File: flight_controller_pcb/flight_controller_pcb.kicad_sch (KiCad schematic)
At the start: 53 parts, among them J1 Conn_01x08, J2 Conn_01x05, J3 Conn_01x02, U1 NRF24L01P-R7, U2 a, U3 STM32F411CEUx, U4 RFX2401C, U5 BMP390, U6 MPU-6500, U7 2450LP14A0100001T, U8 ICM-20948, Y1 Crystal_GND24

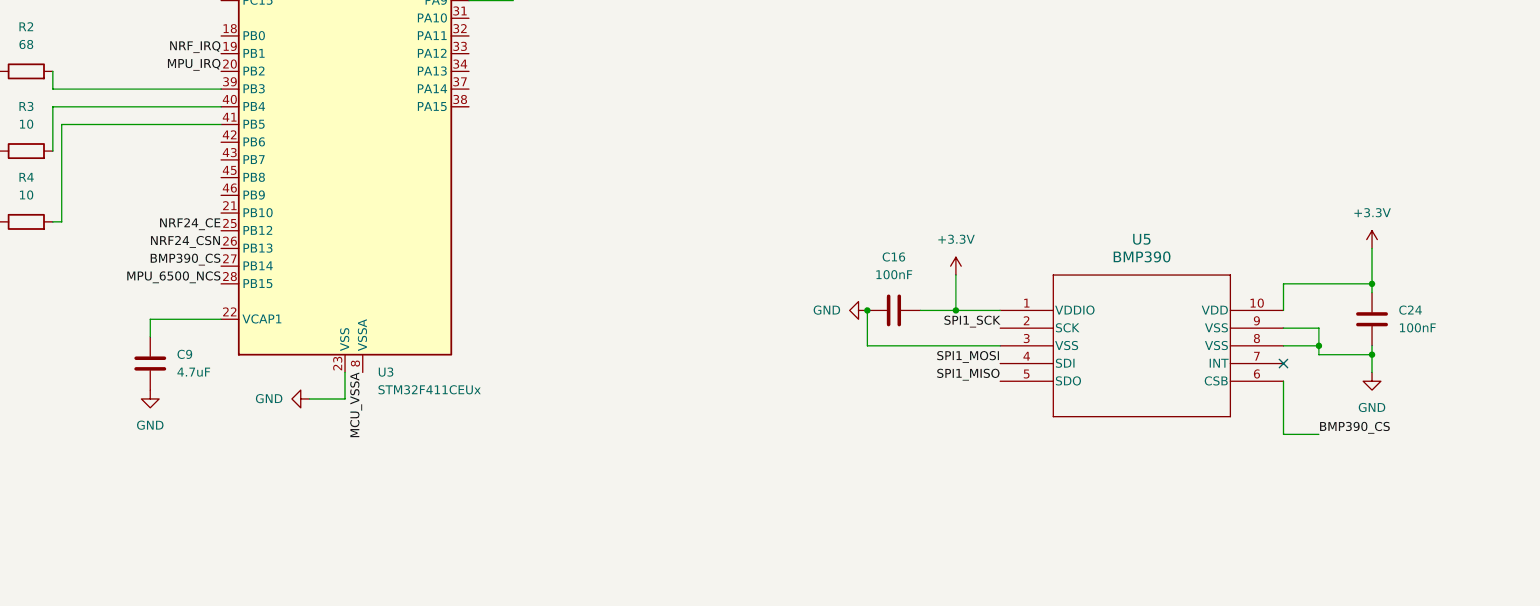
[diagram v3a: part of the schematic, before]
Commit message: Adde interrupt line for bmp390
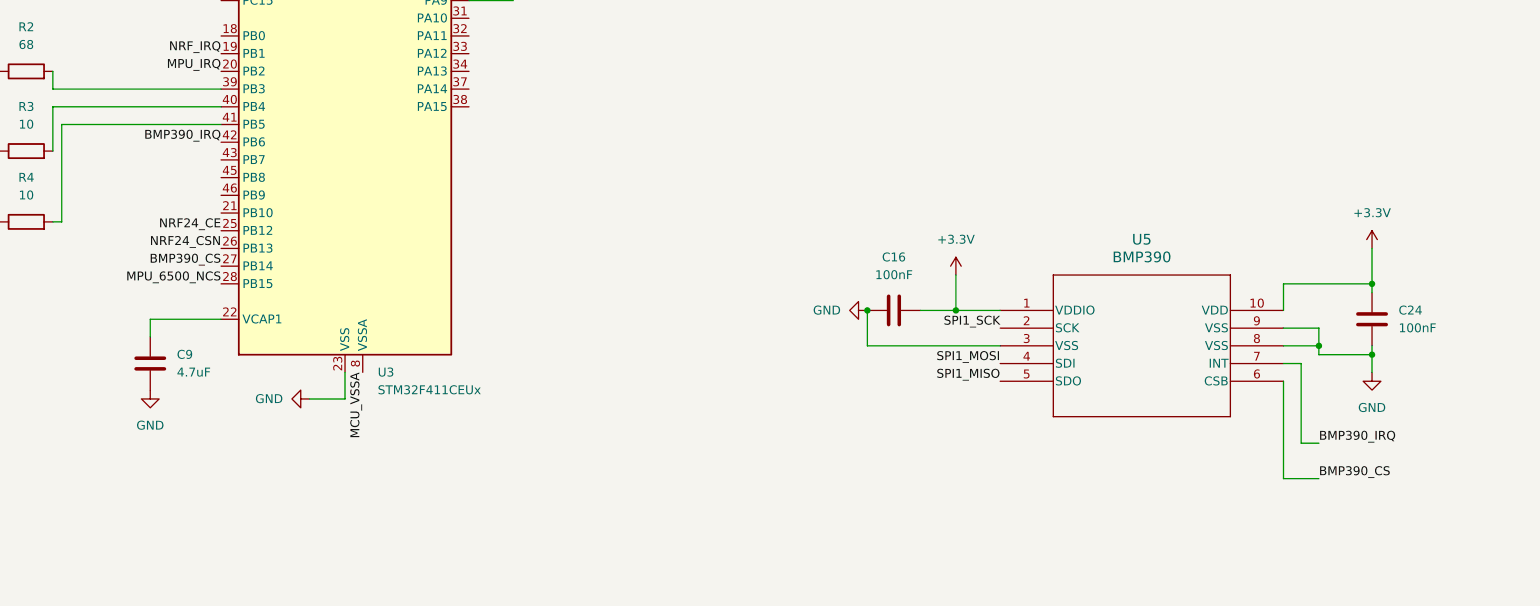
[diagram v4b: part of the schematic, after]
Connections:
- net BMP390_IRQ: now reaches U3.42 (PB6)
- net BMP390_IRQ: now also U5.7 (INT)
- no-connect marks 8 -> 7
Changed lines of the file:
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@@
-	)
-	(no_connect
-		(at 275.59 139.7)
 	)
 	(no_connect
@@
 	(wire
 		(pts
+			(xy 280.67 151.13) (xy 278.13 151.13)
+		)
+		(stroke
+			(width 0)
+			(type default)
+		)
+	)
+	(wire
+		(pts
 			(xy 99.06 109.22) (xy 99.06 102.87)
 		)
@@
 	(wire
 		(pts
-			(xy 275.59 149.86) (xy 280.67 149.86)
+			(xy 275.59 156.21) (xy 280.67 156.21)
 		)
 		(stroke
@@
 	(wire
 		(pts
+			(xy 278.13 139.7) (xy 275.59 139.7)
+		)
+		(stroke
+			(width 0)
+			(type default)
+		)
+	)
+	(wire
+		(pts
 			(xy 82.55 50.8) (xy 87.63 50.8)
 		)
@@
 	(wire
 		(pts
+			(xy 278.13 151.13) (xy 278.13 139.7)
+		)
+		(stroke
+			(width 0)
+			(type default)
+		)
+	)
+	(wire
+		(pts
 			(xy 275.59 53.34) (xy 274.32 53.34)
 		)
@@
 	(wire
 		(pts
-			(xy 275.59 142.24) (xy 275.59 149.86)
+			(xy 275.59 142.24) (xy 275.59 156.21)
 		)
 		(stroke
@@
 		)
 	)
+	(label "BMP390_IRQ"
+		(at 123.19 107.95 180)
+		(effects
+			(font
+				(size 1.27 1.27)
+			)
+			(justify right bottom)
+		)
+	)
 	(label "SPI1_SCK"
 		(at 165.1 77.47 0)
@@
 	)
 	(label "BMP390_CS"
-		(at 280.67 149.86 0)
+		(at 280.67 156.21 0)
 		(effects
 			(font
@@
 		(effects
 			(font
+				(size 1.27 1.27)
+			)
+			(justify left bottom)
+		)
+	)
+	(label "BMP390_IRQ"
+		(at 280.67 151.13 0)
+		(effects
+			(font

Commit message: ALOT of work on the PCB
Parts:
- removed D2: LED_KGBR, symbol Device:LED_KGBR
- removed R4: 10, Resistor_SMD:R_0402_1005Metric, symbol Device:R
- removed U6: MPU-6500, MPU-6500:QFN40P300X300X95-25N, symbol MPU-6500:MPU-6500
- added C25, C26, C27, C28, C29, C30, C31: 0.1uF, Capacitor_SMD:C_0402_1005Metric, symbol Device:C
- added D2, D4: LED, LED_SMD:LED_0402_1005Metric, symbol Device:LED
- added R10: 100K, Resistor_SMD:R_0402_1005Metric, symbol Device:R
- added R11: 1M, Resistor_SMD:R_0402_1005Metric, symbol Device:R
- added U10, U9: SN74LVC2T45YZP, Package_BGA:Texas_DSBGA-8_0.9x1.9mm_Layout2x4_P0.5mm, symbol Logic_LevelTranslator:SN74LVC2T45YZP
- added U11: SN74LVC1T45DRL, Package_TO_SOT_SMD:SOT-563, symbol Logic_LevelTranslator:SN74LVC1T45DRL
- added U6: TLV70018DCKR, TLV70018:DCK5, symbol Texas-Instruments-TLV70018DCKR:TLV70018DCKR
- C13: footprint (none) -> Capacitor_SMD:C_0402_1005Metric
- C22: value 10nF -> 1uF
- C23: value 0.1uF -> 1uF
- C7: value 10uF -> 22uF; footprint (none) -> Capacitor_SMD:C_0805_2012Metric
- D1: footprint (none) -> Diode_SMD:D_SOD-323
- D3: footprint (none) -> fclib:Diode_SMD_SOD-723
- J1: footprint (none) -> fclib:JST_SH_ZX-SH1.0-8PWT
- J2: footprint (none) -> Connector_PinHeader_2.54mm:PinHeader_1x05_P2.54mm_Horizontal
- J3: footprint (none) -> Connector_PinHeader_2.54mm:PinHeader_1x02_P2.54mm_Horizontal
- L1: footprint (none) -> fclib:Inductor_Coilcraft_XFL3012-222MEC
- R2: value 68 -> 270
- R3: value 10 -> 180
- R6, R7: footprint (none) -> Resistor_SMD:R_0402_1005Metric
- U2: value a -> TPS62162
- U8: footprint ICM-20948:QFN40P300X300X105-24N -> ICM_20948:QFN40P300X300X105-24N
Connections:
- net +3.3V: now also C26.2, C28.2, C30.2, U10.A1 (VCCA), U11.1 (VCCA), U6.1 (IN), U6.3 (EN), U9.A1 (VCCA), U9.D2 (DIR)
- net BAT+: now also R10.1
- net ESC1: now also U3.32 (PA11); no longer U3.29 (PA8)
- net ESC2: now also U3.31 (PA10); no longer U3.30 (PA9)
- net ESC3: now also U3.30 (PA9); no longer U3.11 (PA1)
- net ESC4: now also U3.29 (PA8); no longer U3.12 (PA2)
- net GND: now also C22.1, C23.1, U8.11 (FSYNC), U8.20 (RESV_20), C25.2, C26.1, C27.1, C28.1, C29.1, C30.1, C31.1, D2.1 (K), D4.1 (K), R11.2, U10.D1 (GND), U10.D2 (DIR), U11.2 (GND), U11.5 (DIR), U6.2 (GND), U6.4 (NC), U9.D1 (GND); no longer C23.2
- net SPI1_MISO: now also U10.B1 (A1)
- net SPI1_MOSI: now also U9.C1 (A2)
- net SPI1_SCK: now also U9.B1 (A1)
- net at R3.1: now also D4.2 (A)
- net STATUS_LED: now reaches R3.2, U3.40 (PB4)
- net at C1.1, D1.1 (K), U2.2 (VIN): no longer U2.3 (EN)
- net at R2.1: now also D2.2 (A)
- net ERROR_LED: now reaches R2.2, U3.39 (PB3)
- net at U8.10 (REGOUT): now also C25.1
- net ICM_INT_1V8: now reaches U8.12 (INT1)
- net ICM_INT_1V8: now also U10.C2 (B2)
- net ICM_CS_1V8: now reaches U8.22 (~{CS})
- net ICM_CS_1V8: now also U11.4 (B)
- net ICM_SCK: now reaches U8.23 (SCL/SCLK)
- net ICM_SCK: now also U9.B2 (B1)
- net ICM_MOSI: now reaches U8.24 (SDA/SDI)
- net ICM_MOSI: now also U9.C2 (B2)
- net +1V8: now reaches U8.8 (VDDIO)
- net +1V8: now also C23.2, C27.2, C29.2, C31.2, U10.A2 (VCCB), U11.6 (VCCB), U6.5 (OUT), U9.A2 (VCCB)
- net ICM_MISO: now reaches U8.9 (AD0/SDO)
- net ICM_MISO: now also U10.B2 (B1)
- net MPU_6500_NCS renamed ICM_CS_3V3
- net ICM_CS_3V3: now also U11.3 (A)
- net MPU_IRQ renamed ICM_INT_3V3
- net ICM_INT_3V3: now also U10.C1 (A2)
- new net: R10.2, R11.1, U2.3 (EN)
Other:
- note added: "IMU"
- note added: "IMU level shifting, 3.3V <-> 1.8V"
- moved on the sheet: C1, C21, D1, U8

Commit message: alot of work on pcb layout
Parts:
- removed C21: 0.1uF, Capacitor_SMD:C_0402_1005Metric, symbol Device:C
- removed U8: ICM-20948, ICM_20948:QFN40P300X300X105-24N, symbol ICM-20948:ICM-20948
- added C12, C17, C19, C34, C36: 0.1uF, Capacitor_SMD:C_0402_1005Metric, symbol Device:C
- added C16: 4.7uF, Capacitor_SMD:C_0603_1608Metric, symbol Device:C
- added FB1: FerriteBead, Inductor_SMD:L_0603_1608Metric, symbol Device:FerriteBead
- added U11: ICM-20948, Sensor_Motion:InvenSense_QFN-24_3x3mm_P0.4mm, symbol Sensor_Motion:ICM-20948
- C35: renamed from C25; LCSC (none) -> C1525
- J1: LCSC (none) -> C7430450
- renumbered C12 to C13, C13 to C14, C14 to C15, C15 to C18, C22 to C20, C23 to C21, C16 to C22, C17 to C23, C18 to C24, C19 to C25, C20 to C26, C24 to C27, C26 to C28, C28 to C29, C27 to C31, C29 to C32, C31 to C33, D4 to D3, D3 to D4, R9 to R10, R10 to R2, R11 to R3, R2 to R4, R3 to R5, R5 to R6, R6 to R7, R7 to R8, R8 to R9, U11 to U10, U6 to U4, U4 to U5, U5 to U6, U9 to U8, U10 to U9
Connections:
- net +1V8: now also C34.1, C36.2, U11.13 (VDD), U11.8 (VDDIO)
- net +3.3V: now also C12.1, C16.1, C17.1, C19.1, FB1.1; no longer C5.1, C6.1, U3.9 (VDDA)
- net BMP390_CS: now also U3.12 (PA2); no longer U3.27 (PB14)
- net BMP390_IRQ: now also U3.11 (PA1); no longer U3.42 (PB6)
- net ESC1: now also U3.33 (PA12); no longer U3.32 (PA11)
- net ESC2: now also U3.32 (PA11); no longer U3.31 (PA10)
- net ESC3: now also U3.31 (PA10); no longer U3.30 (PA9)
- net ESC4: now also U3.30 (PA9); no longer U3.29 (PA8)
- net GND: now also C12.2, C16.2, C17.2, C19.2, C34.2, C36.1, U11.11 (FSYNC), U11.18 (GND), U11.20 (GND)
- net ICM_CS_1V8: now also U11.22 (~{CS})
- net ICM_CS_3V3: now also U3.21 (PB10); no longer U3.28 (PB15)
- net ICM_INT_1V8: now also U11.12 (INT1)
- net ICM_MISO: now also U11.9 (SDO/AD0)
- net ICM_MOSI: now also U11.24 (SDA/SDI)
- net ICM_SCK: now also U11.23 (SCL/SCLK)
- net NRF24_CSN: now also U3.29 (PA8); no longer U3.26 (PB13)
- net SPI1_MISO: no longer U1.5 (MISO)
- net SPI1_MOSI: no longer U1.4 (MOSI)
- net SPI1_SCK: no longer U1.3 (SCK)
- net at C35.1: now also U11.10 (REGOUT)
- new net MCU_VDDA: C5.1, C6.1, FB1.2, U3.9 (VDDA)
- new net SPI2_MISO: U1.5 (MISO), U3.27 (PB14)
- new net SPI2_MOSI: U1.4 (MOSI), U3.28 (PB15)
- new net SPI2_SCK: U1.3 (SCK), U3.26 (PB13)
- no-connect marks 7 -> 6
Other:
- moved on the sheet: C35

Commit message: routing work
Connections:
- net ESC1: now also U3.34 (PA13); no longer U3.33 (PA12)
- net ESC2: now also U3.33 (PA12); no longer U3.32 (PA11)
- net ESC3: now also U3.32 (PA11); no longer U3.31 (PA10)
- net ESC4: now also U3.31 (PA10); no longer U3.30 (PA9)
- net NRF24_CE: now also U3.30 (PA9); no longer U3.25 (PB12)
- net NRF_IRQ: now also U3.25 (PB12); no longer U3.19 (PB1)

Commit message: more routing
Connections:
- net GND: now also J3.2 (Pin_2); no longer J3.1 (Pin_1)
- net at D4.2 (A): now also J3.1 (Pin_1); no longer J3.2 (Pin_2)
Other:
- moved on the sheet: D4
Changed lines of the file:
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@@
 	)
 	(junction
-		(at 91.44 247.65)
-		(diameter 0)
-		(color 0 0 0 0)
-	)
-	(junction
 		(at 220.98 359.41)
 		(diameter 0)
@@
 	)
 	(junction
+		(at 88.9 247.65)
+		(diameter 0)
+		(color 0 0 0 0)
+	)
+	(junction
 		(at 44.45 386.08)
 		(diameter 0)
@@
 	(wire
 		(pts
-			(xy 85.09 247.65) (xy 91.44 247.65)
+			(xy 85.09 247.65) (xy 88.9 247.65)
 		)
 		(stroke
@@
 	(wire
 		(pts
+			(xy 88.9 247.65) (xy 95.25 247.65)
+		)
+		(stroke
+			(width 0)
+			(type default)
+		)
+	)
+	(wire
+		(pts
 			(xy 213.36 360.68) (xy 215.9 360.68)
 		)
@@
 	(wire
 		(pts
+			(xy 88.9 243.84) (xy 88.9 247.65)
+		)
+		(stroke
+			(width 0)
+			(type default)
+		)
+	)
+	(wire
+		(pts
 			(xy 213.36 381) (xy 215.9 381)
 		)
@@
 	(wire
 		(pts
+			(xy 91.44 233.68) (xy 92.71 233.68)
+		)
+		(stroke
+			(width 0)
+			(type default)
+		)
+	)
+	(wire
+		(pts
 			(xy 158.75 97.79) (xy 165.1 97.79)
 		)
@@
 	(wire
 		(pts
+			(xy 88.9 232.41) (xy 88.9 236.22)
+		)
+		(stroke
+			(width 0)
+			(type default)
+		)
+	)
+	(wire
+		(pts
 			(xy 69.85 69.85) (xy 76.2 69.85)
 		)
@@
 	(wire
 		(pts
-			(xy 91.44 232.41) (xy 91.44 236.22)
-		)
-		(stroke
-			(width 0)
-			(type default)
-		)
-	)
-	(wire
-		(pts
 			(xy 158.75 74.93) (xy 165.1 74.93)
 		)
@@
 	(wire
 		(pts
-			(xy 91.44 247.65) (xy 95.25 247.65)
-		)
-		(stroke
-			(width 0)
-			(type default)
-		)
-	)
-	(wire
-		(pts
 			(xy 49.53 383.54) (xy 49.53 386.08)
 		)
@@
 	(wire
 		(pts
-			(xy 91.44 243.84) (xy 91.44 247.65)
-		)
-		(stroke
-			(width 0)
-			(type default)
-		)
-	)
-	(wire
-		(pts
 			(xy 146.05 54.61) (xy 146.05 57.15)
 		)
@@
 	(wire
 		(pts
+			(xy 91.44 232.41) (xy 91.44 233.68)
+		)
+		(stroke
+			(width 0)
+			(type default)
+		)
+	)
+	(wire
+		(pts
 			(xy 198.12 261.62) (xy 194.31 261.62)
 		)
@@
 	(symbol
 		(lib_id "power:GND")
-		(at 88.9 232.41 0)
+		(at 92.71 233.68 90)
 		(unit 1)
 		(exclude_from_sim no)
@@
 		(fields_autoplaced yes)
 		(property "Reference" "#PWR018"
-			(at 88.9 238.76 0)
+			(at 99.06 233.68 0)
 			(effects
 				(font
@@
 		)
 		(property "Value" "GND"
-			(at 88.9 237.49 0)
+			(at 96.52 233.6799 90)
 			(effects
 				(font
 					(size 1.27 1.27)
 				)
+				(justify right)
 			)
 		)
 		(property "Footprint" ""
-			(at 88.9 232.41 0)
+			(at 92.71 233.68 0)
 			(effects
 				(font
@@
 		)
 		(property "Datasheet" ""
-			(at 88.9 232.41 0)
+			(at 92.71 233.68 0)
 			(effects
 				(font
@@
 		)
 		(property "Description" "Power symbol creates a global label with name \"GND\" , ground"
-			(at 88.9 232.41 0)
+			(at 92.71 233.68 0)
 			(effects
 				(font
@@
 	(symbol
 		(lib_id "Device:D_Schottky")
-		(at 91.44 240.03 90)
+		(at 88.9 240.03 90)
 		(unit 1)
 		(exclude_from_sim no)
@@
 		(fields_autoplaced yes)
 		(property "Reference" "D4"
-			(at 93.98 239.0774 90)
+			(at 91.44 239.0774 90)
 			(effects
 				(font
@@
 		)
 		(property "Value" "D_Schottky"
-			(at 93.98 241.6174 90)
+			(at 91.44 241.6174 90)
 			(effects
 				(font
@@
 		)
 		(property "Footprint" "fclib:Diode_SMD_SOD-723"
-			(at 91.44 240.03 0)
+			(at 88.9 240.03 0)
 			(effects
 				(font
@@
 		)
 		(property "Datasheet" "~"
-			(at 91.44 240.03 0)
+			(at 88.9 240.03 0)
 			(effects
 				(font
@@
 		)
 		(property "Description" "Schottky diode (C8526 or C116010 for lead-free)"
-			(at 91.44 240.03 0)
+			(at 88.9 240.03 0)
 			(effects
 				(font
